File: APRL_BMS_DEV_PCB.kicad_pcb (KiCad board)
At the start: 4 copper layers, 73 parts, among them J1 Conn_01x04_Pin, J3 Conn_01x02_Pin, J4 Conn_01x08_Pin, J5 Conn_01x01_Pin, Q1 Q_NPN, SW1 SW_SPDT, U1 BQ756506-Q1, U2 STM32F446RCTx, U3 ISO7741DWR, Y1 20MHz

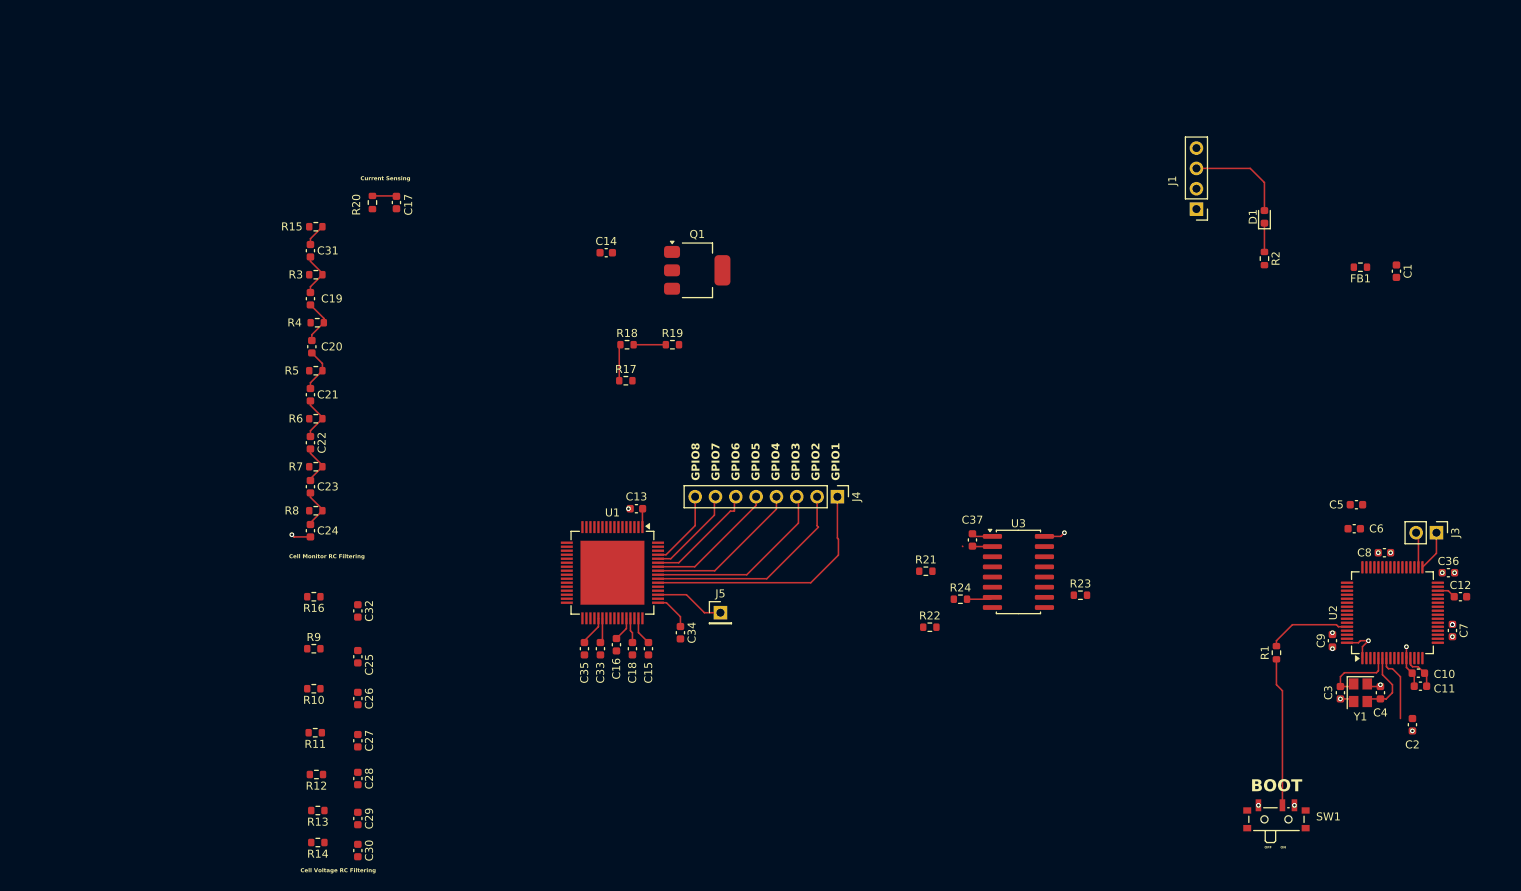
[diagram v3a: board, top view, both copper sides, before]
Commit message: Fixed TX and RX Trace distances
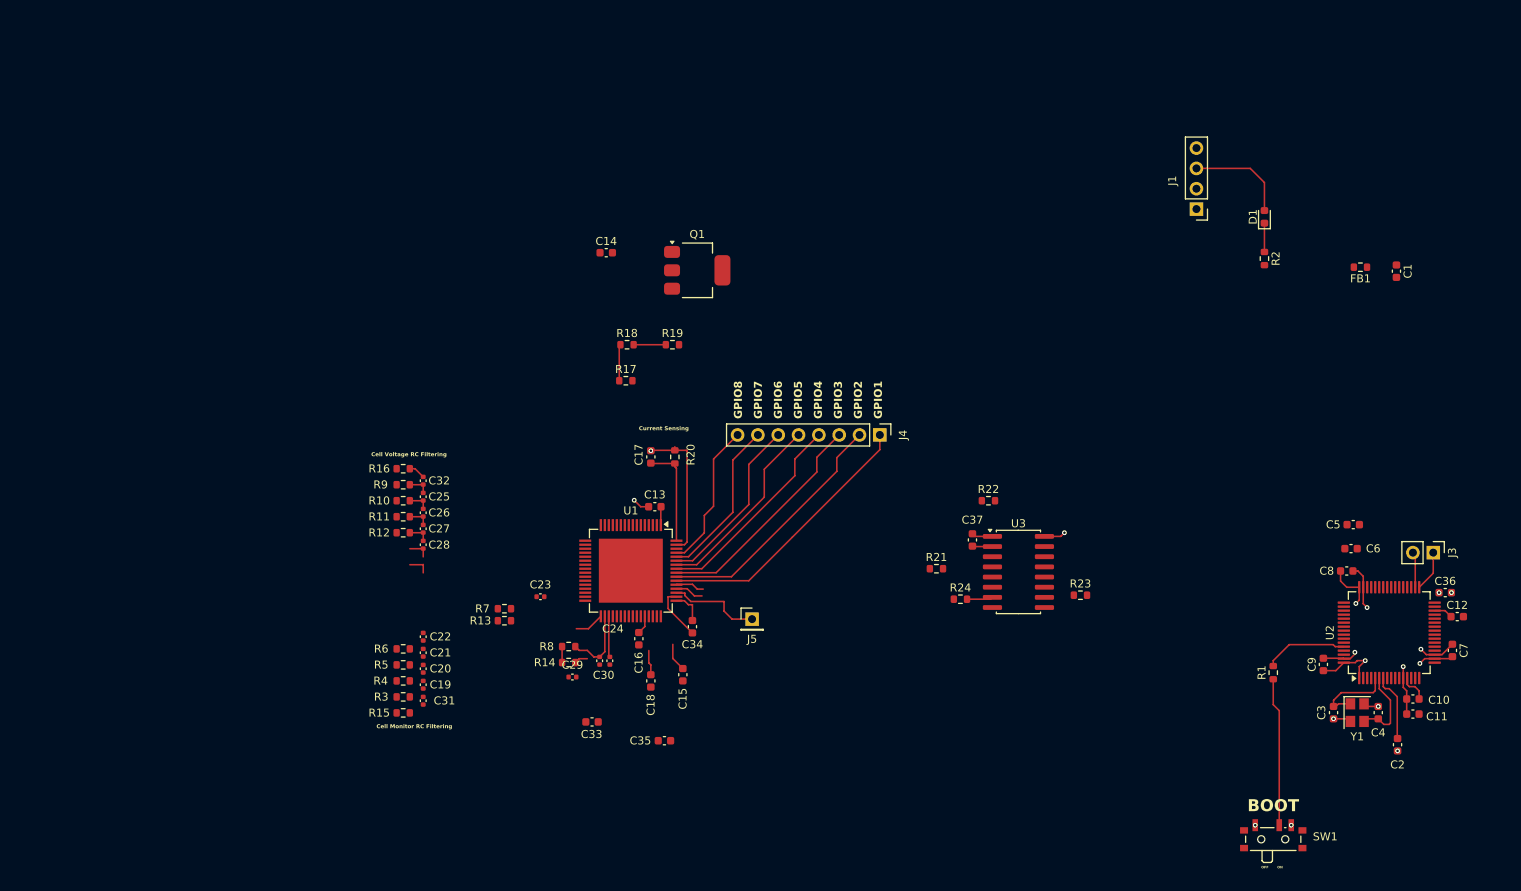
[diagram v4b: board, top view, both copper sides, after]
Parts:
- C19, C20, C21, C22, C23, C24, C25, C26, C27, C28, C29, C30, C31, C32: footprint Capacitor_SMD:C_0603_1608Metric -> Capacitor_SMD:C_0402_1005Metric
- moved R15 61.7 mm to (96.3, 118.0)
- moved C31 58.0 mm to (98.8, 116.5), turned to 90 degrees
- moved R3 53.9 mm to (96.3, 116.0)
- moved C19 50.3 mm to (98.8, 114.5), turned to 90 degrees
- moved R20 49.4 mm to (130.3, 86.0), turned to 90 degrees
- moved R4 46.0 mm to (96.3, 114.0)
- moved C17 45.0 mm to (127.3, 86.0), turned to 90 degrees
- moved C20 42.6 mm to (98.8, 112.5), turned to 90 degrees
- moved C24 39.6 mm to (120.9, 111.5)
- moved C30 39.4 mm to (122.2, 111.5)
- moved R14 38.6 mm to (117.0, 111.7)
- moved R5 38.4 mm to (96.3, 112.0)
- moved R8 35.9 mm to (117.0, 109.7)
- moved C21 35.2 mm to (98.8, 110.5), turned to 90 degrees
- moved R13 33.3 mm to (109.0, 106.5)
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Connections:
- net Net-(J1-Pin_1) renamed /SWDIO
- C16 pad 1: GND -> /CVSS
- C18 pad 2: GND -> /CVSS
- C33 pad 1: GND -> /AVSS
- C34 pad 2: GND -> /DVSS
- C35 pad 2: GND -> /REFHM
- U1 pad 36: GND -> /REFHM
- U1 pad 39: GND -> /AVSS
- U1 pad 46: GND -> /CVSS
- U1 pad 50: GND -> /DVSS
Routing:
- net GND: track 15.8 -> 48.8 mm
- net +3.3V: track 21.4 -> 34.8 mm, vias 8 -> 6
- net /CELL_0: track 3.23 -> 14.8 mm
- net /VC0: track 0.00 -> 9.55 mm
- net /GPIO8: track 9.76 -> 18.5 mm
- net /GPIO7: track 11.7 -> 20.3 mm
- net /GPIO6: track 14.1 -> 22.2 mm
- net /GPIO5: track 16.5 -> 24.0 mm
- net /DVSS: track 0.00 -> 6.81 mm
- net /VC1: track 0.00 -> 6.44 mm
- net /GPIO4: track 19.5 -> 26.0 mm
- net /CB4: track 5.77 -> 0.00 mm
- net /CB5: track 5.69 -> 0.00 mm
- net /CB2: track 5.69 -> 0.00 mm
- net /CB3: track 5.62 -> 0.00 mm
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
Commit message: Started routing Vias for voltage sensing pins
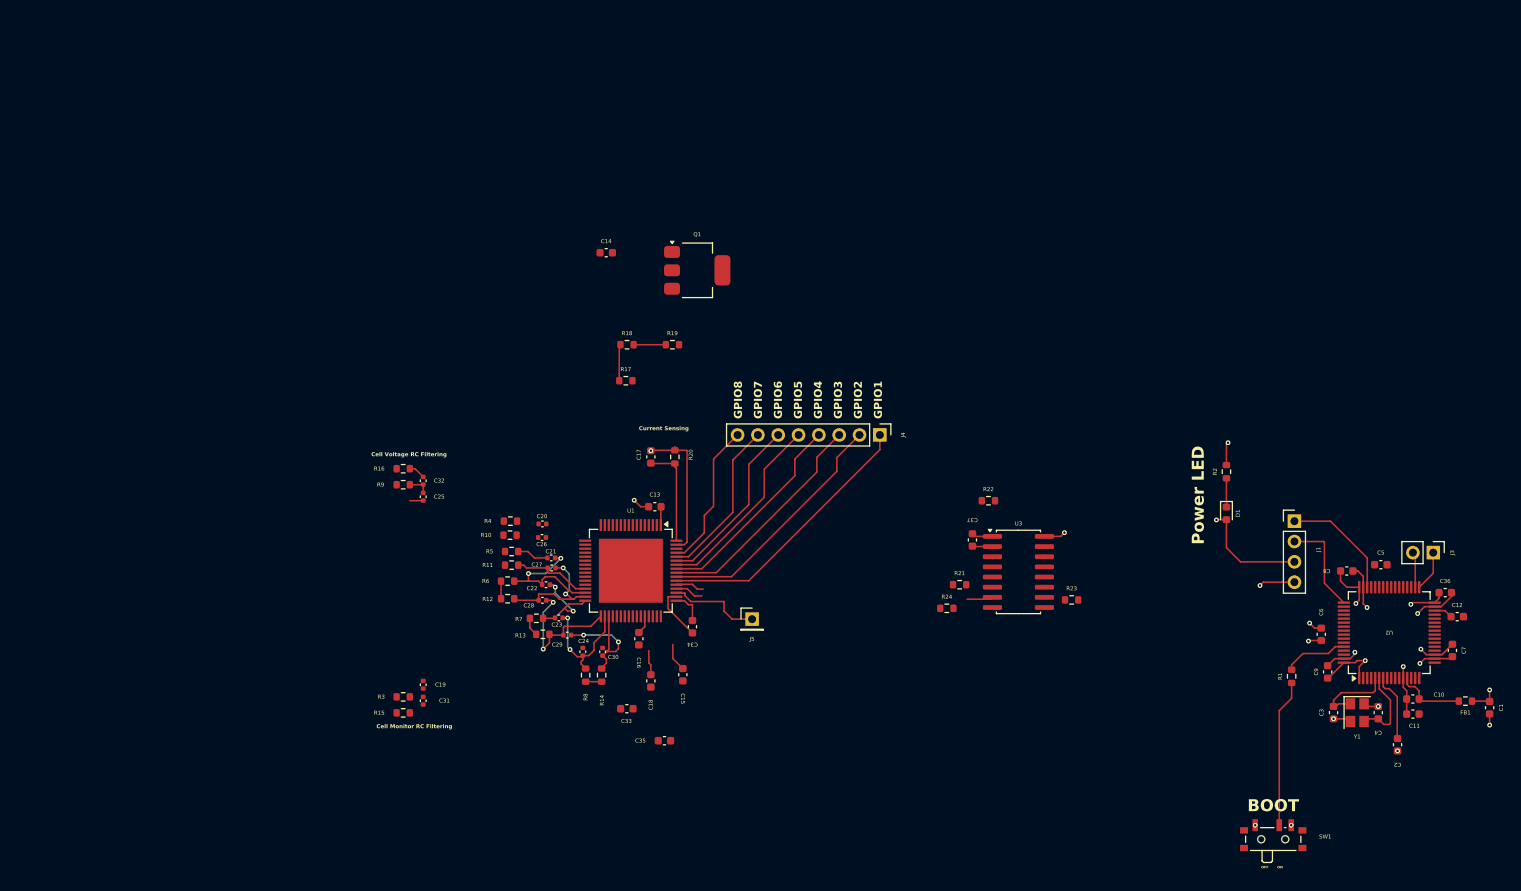
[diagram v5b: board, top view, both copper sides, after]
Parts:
- moved FB1 55.8 mm to (229.1, 116.5)
- moved C1 55.8 mm to (232.2, 117.4)
- moved J1 40.9 mm to (207.8, 94.1), turned to 0 degrees
- moved D1 37.4 mm to (199.2, 93.1), turned to -90 degrees
- moved R2 27.1 mm to (199.2, 87.9), turned to 90 degrees
- moved R4 24.1 mm to (109.8, 94.0)
- moved C20 23.4 mm to (113.8, 94.4), turned to 0 degrees
- moved C21 19.9 mm to (114.8, 98.7), turned to 0 degrees
- moved R5 19.6 mm to (109.9, 97.8)
- moved C27 16.8 mm to (114.9, 99.9), turned to 0 degrees
- moved C22 16.7 mm to (114.2, 102.0), turned to 0 degrees
- moved C28 16.4 mm to (113.8, 104.0), turned to 0 degrees
- moved R6 15.6 mm to (109.4, 101.5)
- moved R12 15.4 mm to (109.4, 103.8)
- moved C26 15.2 mm to (113.7, 96.1), turned to 0 degrees
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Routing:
- net /CB2: track 0.00 -> 17.3 mm, vias 0 -> 2
- net GND: track 48.8 -> 64.2 mm, vias 11 -> 15
- net /SWDIO: track 0.00 -> 14.7 mm
- net /VC2: track 2.72 -> 16.0 mm, vias 0 -> 2
- net /SWCLK: track 0.00 -> 12.3 mm
- net /CB1: track 0.00 -> 12.2 mm, vias 0 -> 2
- net /VC1: track 6.44 -> 17.6 mm, vias 0 -> 2
- net +3.3V: track 34.8 -> 45.8 mm, vias 6 -> 9
- net /VC3: track 2.72 -> 9.93 mm
- net /VC0: track 9.55 -> 16.2 mm, vias 0 -> 2
- net /CB0: track 8.93 -> 15.1 mm, vias 0 -> 2
- net +3.3VA: track 4.04 -> 9.12 mm
- net /CB3: track 0.00 -> 3.98 mm
- net /BOOT0: track 10.4 -> 8.08 mm
- net /CELL_1: track 0.00 -> 2.33 mm
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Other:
- board text added: "Power LED"

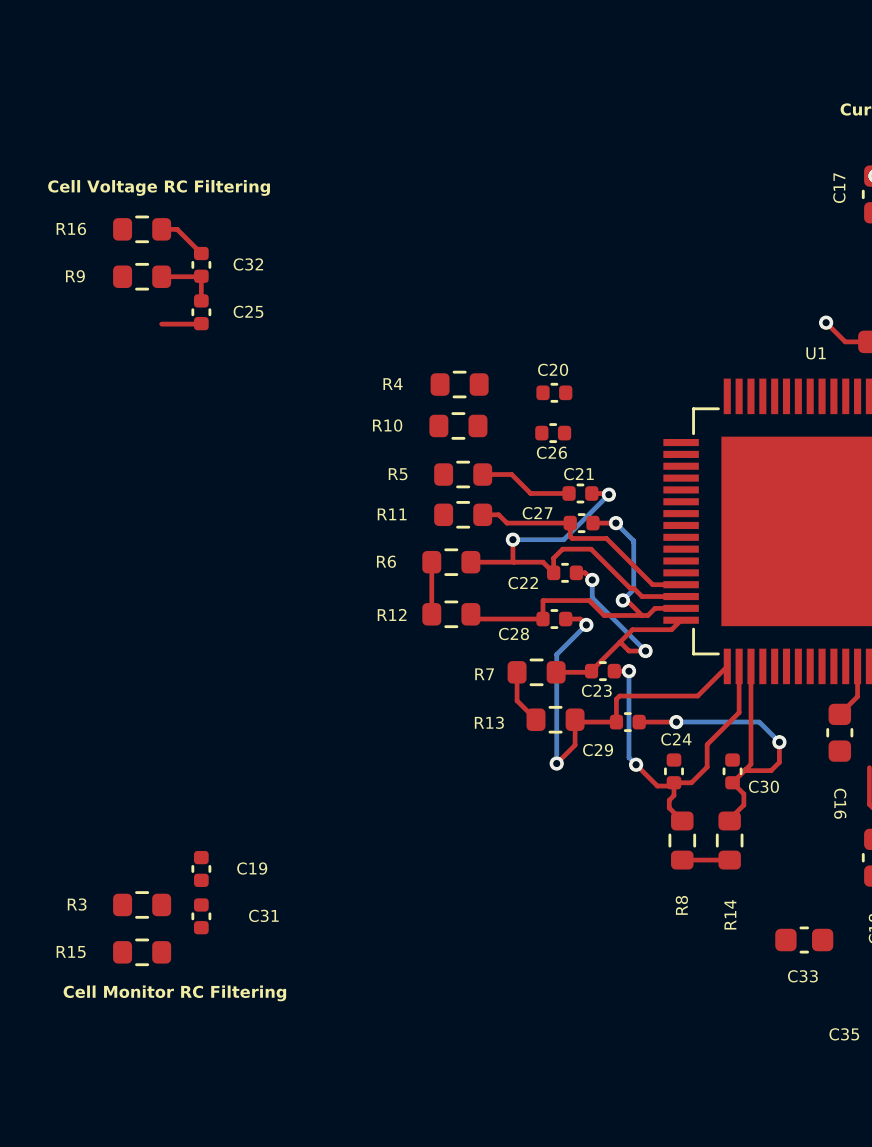
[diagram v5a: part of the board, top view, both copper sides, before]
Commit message: Changed trace width for signals to 0.15mm
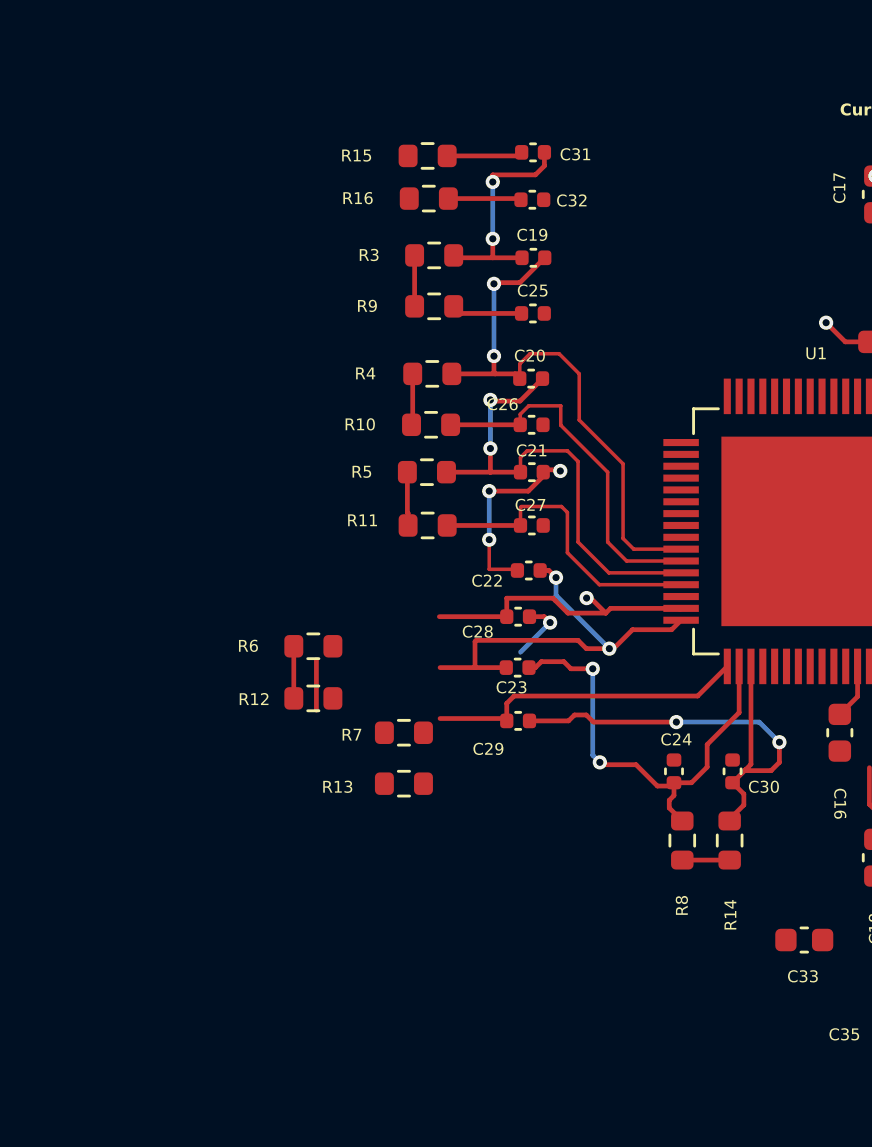
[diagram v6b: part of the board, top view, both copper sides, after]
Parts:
- moved R15 35.7 mm to (108.4, 84.4)
- moved C31 35.2 mm to (112.8, 84.2), turned to 0 degrees
- moved R3 30.1 mm to (108.7, 88.6)
- moved C19 29.4 mm to (112.9, 88.7), turned to 0 degrees
- moved C32 14.2 mm to (112.8, 86.2), turned to 0 degrees
- moved C25 14.0 mm to (112.8, 91.0), turned to 0 degrees
- moved R9 12.4 mm to (108.7, 90.8)
- moved R16 12.2 mm to (108.5, 86.2)
- moved R13 6.95 mm to (107.4, 110.9)
- moved R12 6.82 mm to (103.6, 107.3)
- moved R6 6.82 mm to (103.6, 105.1)
- moved R7 6.15 mm to (107.4, 108.8)
- moved C29 4.63 mm to (112.2, 108.2)
- moved C23 3.60 mm to (112.2, 106.0)
- moved C21 2.24 mm to (112.8, 97.8)
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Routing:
- net /CB4: track 0.00 -> 23.4 mm, vias 0 -> 2
- net /CB3: track 3.98 -> 20.4 mm, vias 0 -> 2
- net /VC4: track 1.68 -> 15.2 mm
- net /CB5: track 0.00 -> 9.33 mm, vias 0 -> 2
- net /CB2: track 17.3 -> 8.03 mm, vias 2 -> 3
- net /CB1: track 12.2 -> 18.0 mm
- net /VC0: track 16.2 -> 21.0 mm
- net /CB0: track 15.1 -> 19.0 mm
- net /VC2: track 16.0 -> 12.8 mm, vias 2 -> 1
- net /CB6: track 0.00 -> 3.21 mm
- net /VC3: track 9.93 -> 13.0 mm
- net /CELL_3: track 0.00 -> 2.26 mm
- net /CELL_5: track 0.00 -> 2.15 mm
- net /CELL_4: track 0.00 -> 1.77 mm
- net /VC1: track 17.6 -> 16.3 mm, vias 2 -> 1
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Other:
- board text removed: "Cell Monitor RC Filtering"
- board text removed: "Cell Voltage RC Filtering"
